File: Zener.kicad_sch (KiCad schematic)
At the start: 15 parts, among them J1 Conn_02x05_Counter_Clockwise, U1 TMP236

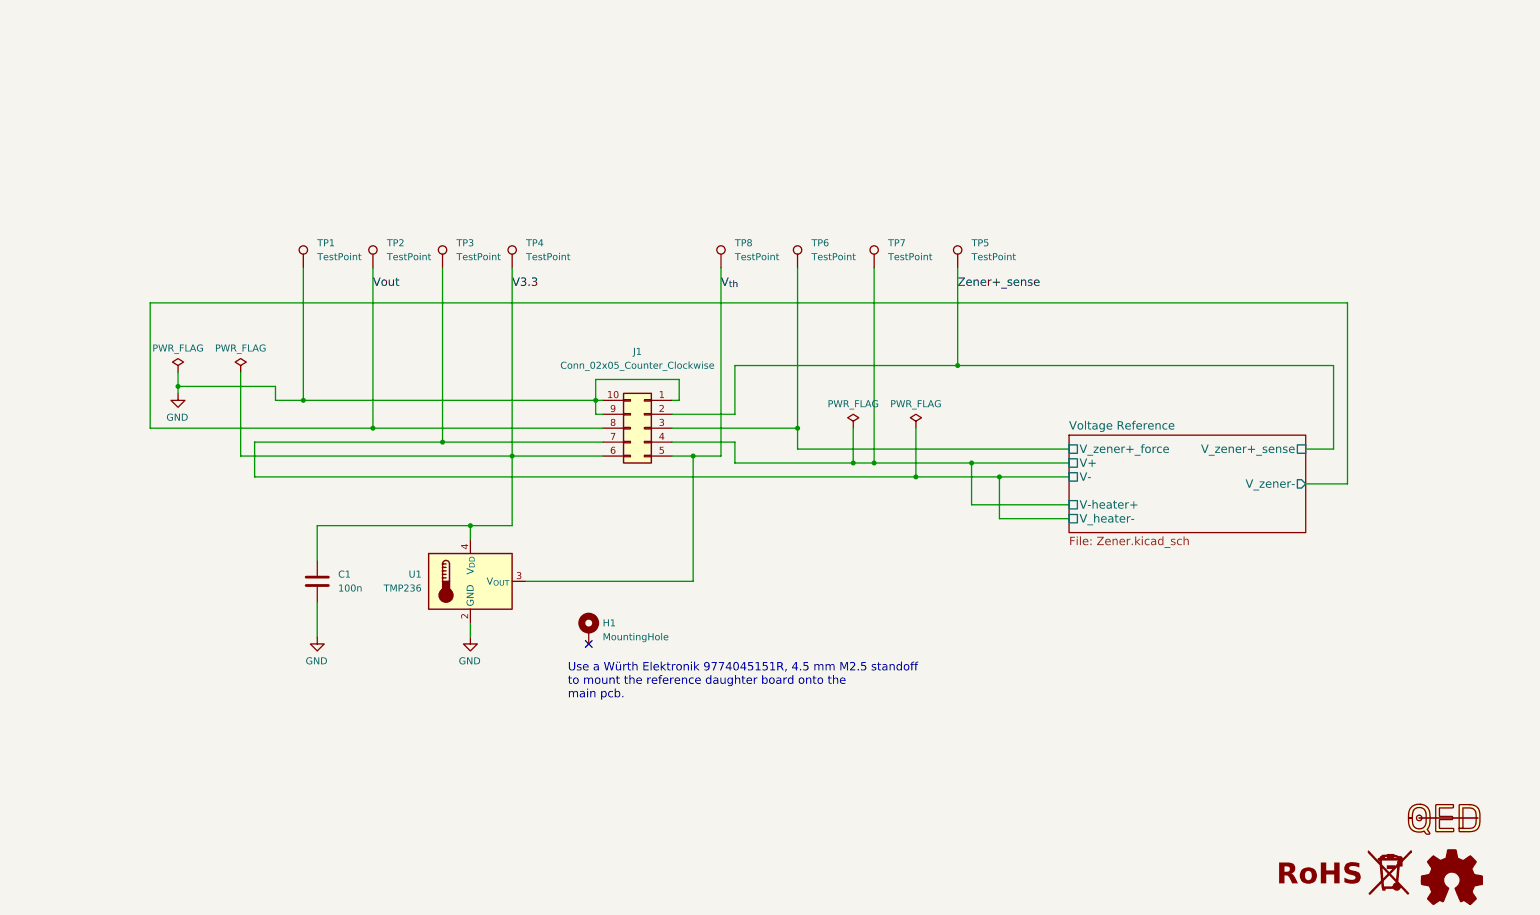
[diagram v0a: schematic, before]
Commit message: Update/connector (#1)
* Replaced connector J1 with Molex SlimStack 53307-1071.

- Updated to KiCAD 10
- Changed BAS116 diode D1 footprint to SOD-123F due to availability of parts
- Added QED logo
- Removed most references to LM399. The ADR1399 is now the default. LM399 is mentioned as option.
- Added more details for different zener voltage configurations
- Added WEEE logo
- Fixed label on silkscreen refering to R1 instead of R2. It now reads 'R2: 10 ppm/K max.'

* Change standoff to WE 9774045151R.

* Changed silkscreen colour to black

* Bump version to 4.0.0

* Updated symbol

- Added WEEE logo

* Update readme

* Updated CI
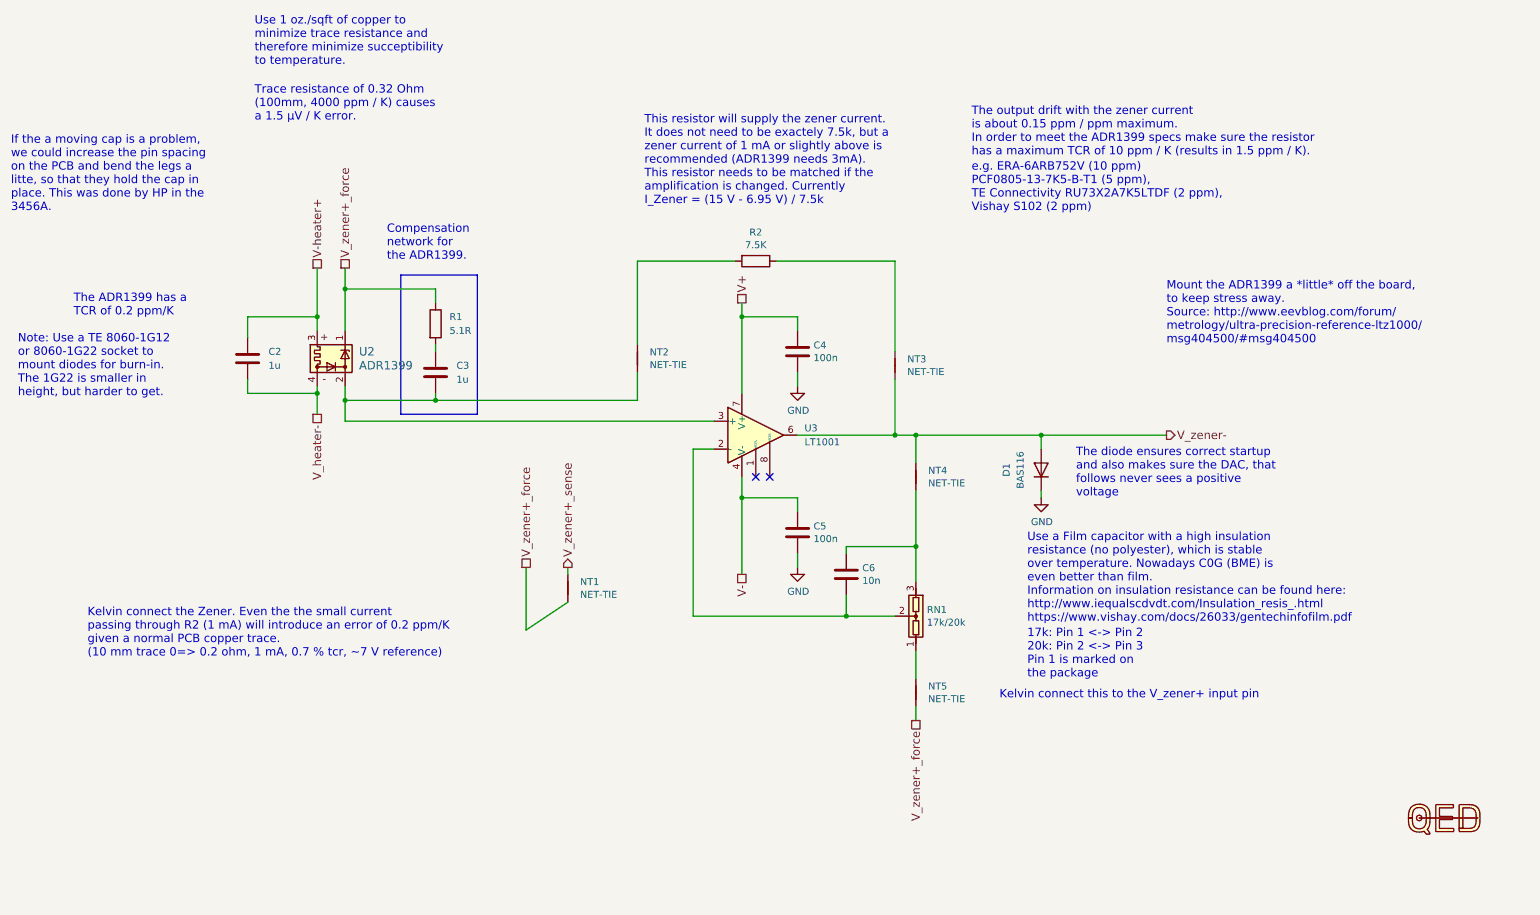
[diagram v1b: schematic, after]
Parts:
- removed C1: 100n, Capacitor_SMD:C_0603_1608Metric, symbol Device:C
- removed H1: MountingHole, MountingHole:MountingHole_2.7mm_M2.5_DIN965_Pad, symbol Mechanical:MountingHole_Pad
- removed J1: Conn_02x05_Counter_Clockwise, Custom_footprints_project:Molex_SlimStack_53307-1071_2x05_P0.80mm_Vertical, symbol Connector_Generic:Conn_02x05_Counter_Clockwise
- removed LOGO1: Logo_Open_Hardware_Small, Symbol:OSHW-Logo2_7.3x6mm_SilkScreen, symbol Graphic:Logo_Open_Hardware_Small
- removed LOGO2: Logo_QED, Custom_footprints_project:QED-logo_small, symbol Custom_logos:Logo_QED
- removed SYM2: SYM_WEEE, Symbol:WEEE-Logo_4.2x6mm_SilkScreen, symbol Custom_logos:SYM_WEEE
- removed TP1, TP2, TP3, TP4, TP5, TP6, TP7, TP8: TestPoint, TestPoint:TestPoint_Pad_D1.5mm, symbol Connector:TestPoint
- removed U1: TMP236, Package_TO_SOT_SMD:SOT-353_SC-70-5, symbol Sensor_Temperature:TMP20AIDCK
- added C2, C3: 1u, Capacitor_SMD:C_0603_1608Metric, symbol Device:C
- added C4, C5: 100n, Capacitor_SMD:C_0603_1608Metric, symbol Device:C
- added C6: 10n, Capacitor_SMD:C_0603_1608Metric, symbol Device:C
- added D1: BAS116, Diode_SMD:D_SOD-123F, symbol Device:D
- added NT1: NET-TIE, Custom_footprints:NET-TIE-0.15mm, symbol Device:NetTie_2
- added NT2, NT3, NT4, NT5: NET-TIE, Custom_footprints:NET-TIE-0.25mm, symbol Device:NetTie_2
- added R1: 5.1R, Resistor_SMD:R_0603_1608Metric, symbol Device:R
- added R2: 7.5K, Resistor_SMD:R_0805_2012Metric, symbol Device:R
- added RN1: 17k/20k, Custom_footprints:R_Array_Box3_L7.5mm_W2.5mm_P2.54mm_Vishay_300144, symbol Device:VoltageDivider
- added U2: ADR1399, Package_TO_SOT_THT:Analog_TO-46-4_ThermalShield, symbol Reference_Voltage:LM399
- added U3: LT1001, Package_SO:SOIC-8_3.9x4.9mm_P1.27mm, symbol Amplifier_Operational:OP07
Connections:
- net GND: now also C4.2, C5.2, D1.1 (K)
- new net: C3.2, NT2.2, U2.2, U3.3 (+)
- new net: NT3.1, R2.1
- new net: NT2.1, R2.2
- new net: C6.1, NT4.2, RN1.3
- new net: C6.2, RN1.2, U3.2 (-)
- new net: NT5.1, RN1.1
- new net: C3.1, R1.2
- new net V+: C4.1, U3.7 (V+)
- new net V-: C5.1, U3.4 (V-)
- new net V-heater+: C2.1, U2.3
- new net V_heater-: C2.2, U2.4
- new net V_zener+_force: NT1.2, NT5.2, R1.1, U2.1
- new net V_zener+_sense: NT1.1
- new net V_zener-: D1.2 (A), NT3.2, NT4.1, U3.6
- no-connect marks 1 -> 2
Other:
- removed sheet Voltage Reference
- note added: "17k: Pin 1 <-> Pin 2 20k: Pin 2 <-> Pin 3 Pin 1 is marked on the package"
- note added: "Compensation network for the ADR1399."
- note added: "If the a moving cap is a problem, we could increase the pin spacing on the PCB and bend the legs a litte, so that they hold the cap in place. This was done by HP in the 3456A."
- note added: "Kelvin connect the Zener. Even the the small current passing through R2 (1 mA) will introduce an error of 0.2 ppm/K given a normal PCB copper trace. (10 mm trace 0=> 0.2 ohm, 1 mA, 0.7 % tcr, ~7 V reference)"
- note added: "Kelvin connect this to the V_zener+ input pin"
- note added: "Mount the ADR1399 a *little* off the board, to keep stress away. Source: http://www.eevblog.com/forum/ metrology/ultra-precision-reference-ltz1000/ msg404500/#msg404500"
- note added: "Note: Use a TE 8060-1G12 or 8060-1G22 socket to mount diodes for burn-in. The 1G22 is smaller in height, but harder to get."
- note added: "The ADR1399 has a TCR of 0.2 ppm/K"
- note added: "The diode ensures correct startup and also makes sure the DAC, that follows never sees a positive voltage"
- note added: "The output drift with the zener current is about 0.15 ppm / ppm maximum. In order to meet the ADR1399 specs make sure the resistor has a maximum TCR of 10 ppm / K (results in 1.5 ppm / K)."
- note added: "This resistor will supply the zener current. It does not need to be exactely 7.5k, but a zener current of 1 mA or slightly above is recommended (ADR1399 needs 3mA). This resistor needs to be matched if the amplification is changed. Currently I_Zener = (15 V - 6.95 V) / 7.5k"
- note added: "Trace resistance of 0.32 Ohm (100mm, 4000 ppm / K) causes a 1.5 µV / K error."
- note added: "Use 1 oz./sqft of copper to minimize trace resistance and therefore minimize succeptibility to temperature."
- note added: "Use a Film capacitor with a high insulation resistance (no polyester), which is stable over temperature. Nowadays C0G (BME) is even better than film. Information on insulation resistance can be found here: http://www.iequalscdvdt.com/Insulation_resis_.html https://www.vishay.com/docs/26033/gentechinfofilm.pdf"
- note added: "e.g. ERA-6ARB752V (10 ppm) PCF0805-13-7K5-B-T1 (5 ppm), TE Connectivity RU73X2A7K5LTDF (2 ppm), Vishay S102 (2 ppm)"
- note removed: "Use a Würth Elektronik 9774045151R, 4.5 mm M2.5 standoff to mount the reference daughter board onto the main pcb."
